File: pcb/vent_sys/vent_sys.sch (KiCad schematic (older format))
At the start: 22 parts

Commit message: deleted ds2482-100
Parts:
- removed J?: Conn_01x03_Female, symbol Connector:Conn_01x03_Female
- removed R?: R_Variable, symbol Device:R_Variable
- removed R? (x2): R, symbol Device:R
- removed U?: DS2482-100, Housings_SOIC:SOIC-8_3.9x4.9mm_Pitch1.27mm, symbol maxim:DS2482-100
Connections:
- wire segments 145 -> 115
- no-connect marks 1 -> 0
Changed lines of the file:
@@
 Wire Bus Line
 	8000 2100 10800 2100
-$Comp
-L maxim:DS2482-100 U?
-U 1 1 5C5AE47D
-P 2600 1300
-F 0 "U?" H 2600 1978 50  0000 C CNN
-F 1 "DS2482-100" H 2600 1887 50  0000 C CNN
-F 2 "Housings_SOIC:SOIC-8_3.9x4.9mm_Pitch1.27mm" H 2650 900 50  0001 L CNN
-F 3 "https://datasheets.maximintegrated.com/en/ds/DS2482-100.pdf" H 2870 1550 50  0001 C CNN
-	1    2600 1300
-	1    0    0    -1
-$EndComp
-$Comp
-L Device:R_Variable R?
-U 1 1 5C5AE99F
-P 3400 1150
-F 0 "R?" H 3528 1196 50  0000 L CNN
-F 1 "R_Variable" H 3528 1105 50  0000 L CNN
-F 2 "" V 3330 1150 50  0001 C CNN
-F 3 "~" H 3400 1150 50  0001 C CNN
-	1    3400 1150
-	1    0    0    -1
-$EndComp
-$Comp
-L Device:R R?
-U 1 1 5C5AEA85
-P 800 1000
-F 0 "R?" H 870 1046 50  0000 L CNN
-F 1 "R" H 870 955 50  0000 L CNN
-F 2 "" V 730 1000 50  0001 C CNN
-F 3 "~" H 800 1000 50  0001 C CNN
-	1    800  1000
-	1    0    0    -1
-$EndComp
-$Comp
-L Connector:Conn_01x03_Female J?
-U 1 1 5C5B0332
-P 4000 1400
-F 0 "J?" H 4027 1426 50  0000 L CNN
-F 1 "Conn_01x03_Female" H 4027 1335 50  0000 L CNN
-F 2 "" H 4000 1400 50  0001 C CNN
-F 3 "~" H 4000 1400 50  0001 C CNN
-	1    4000 1400
-	1    0    0    -1
-$EndComp
-$Comp
-L power:+3.3V #PWR?
-U 1 1 5C5B7267
-P 2950 700
-F 0 "#PWR?" H 2950 550 50  0001 C CNN
-F 1 "+3.3V" H 2965 873 50  0000 C CNN
-F 2 "" H 2950 700 50  0001 C CNN
-F 3 "" H 2950 700 50  0001 C CNN
-	1    2950 700
-	1    0    0    -1
-$EndComp
-Wire Wire Line
-	2600 800  2950 800
-Wire Wire Line
-	2950 800  2950 750
-$Comp
-L power:GND #PWR?
-U 1 1 5C5B77FB
-P 2600 1950
-F 0 "#PWR?" H 2600 1700 50  0001 C CNN
-F 1 "GND" H 2605 1777 50  0000 C CNN
-F 2 "" H 2600 1950 50  0001 C CNN
-F 3 "" H 2600 1950 50  0001 C CNN
-	1    2600 1950
-	1    0    0    -1
-$EndComp
-Wire Wire Line
-	2600 1800 2600 1850
-NoConn ~ 3100 1100
-$Comp
-L Device:R R?
-U 1 1 5C5B9E9D
-P 1400 1000
-F 0 "R?" H 1470 1046 50  0000 L CNN
-F 1 "R" H 1470 955 50  0000 L CNN
-F 2 "" V 1330 1000 50  0001 C CNN
-F 3 "~" H 1400 1000 50  0001 C CNN
-	1    1400 1000
-	1    0    0    -1
-$EndComp
-Wire Wire Line
-	1400 750  2950 750
-Connection ~ 2950 750
-Wire Wire Line
-	3400 750  2950 750
-Wire Wire Line
-	2950 750  2950 700
-Wire Wire Line
-	1400 850  1400 750
-Connection ~ 1400 750
-Wire Wire Line
-	800  750  1400 750
-Wire Wire Line
-	2100 1100 1700 1100
-Wire Wire Line
-	1700 1100 1700 1150
-Wire Wire Line
-	1700 1150 1400 1150
-Wire Wire Line
-	800  850  800  750
-Wire Wire Line
-	800  1150 800  1250
-Wire Wire Line
-	800  1250 1900 1250
-Wire Wire Line
-	1900 1250 1900 1200
-Wire Wire Line
-	1900 1200 2100 1200
-$Comp
-L power:GND #PWR?
-U 1 1 5C5C0A5C
-P 1600 1550
-F 0 "#PWR?" H 1600 1300 50  0001 C CNN
-F 1 "GND" H 1605 1377 50  0000 C CNN
-F 2 "" H 1600 1550 50  0001 C CNN
-F 3 "" H 1600 1550 50  0001 C CNN
-	1    1600 1550
-	1    0    0    -1
-$EndComp
-Wire Wire Line
-	2100 1400 1600 1400
-Wire Wire Line
-	1600 1400 1600 1500
-Wire Wire Line
-	2100 1500 1600 1500
-Connection ~ 1600 1500
-Wire Wire Line
-	1600 1500 1600 1550
-Wire Wire Line
-	3400 1000 3400 750
-Connection ~ 3400 750
-Wire Wire Line
-	3700 750  3400 750
-Wire Wire Line
-	3100 1400 3400 1400
-Wire Wire Line
-	3400 1400 3400 1300
-Connection ~ 3400 1400
-Wire Wire Line
-	3800 1400 3400 1400
-Wire Wire Line
-	3800 1500 3800 1850
-Wire Wire Line
-	3800 1850 2600 1850
-Connection ~ 2600 1850
-Wire Wire Line
-	2600 1850 2600 1950
-Wire Wire Line
-	3800 1300 3700 1300
-Wire Wire Line
-	3700 1300 3700 750
 $EndSCHEMATC

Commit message: connect RA02
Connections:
- net Reset: now reaches U?.26 (A1)
- net Reset: now also U?.4 (reset)
- net nIRQ: now reaches U?.27 (A2/U2TX)
- net nIRQ: now also U?.5 (dio0)
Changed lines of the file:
@@
 Text Label 4200 1700 0    50   ~ 0
 Herz_counter
+Entry Wire Line
+	9200 2100 9300 2200
+Wire Wire Line
+	8500 1200 8000 1200
+Wire Wire Line
+	8000 1200 8000 2000
+Entry Wire Line
+	8000 2000 8100 2100
+Text Label 7300 3800 0    50   ~ 0
+Reset
+Text Label 8050 1200 0    50   ~ 0
+Reset
+Wire Wire Line
+	6750 3800 9300 3800
+Wire Wire Line
+	9300 3800 9300 2200
+Entry Wire Line
+	9100 2100 9200 2200
+Wire Wire Line
+	9200 2200 9200 3650
+Wire Wire Line
+	9200 3650 6750 3650
+Text Label 7300 3650 0    50   ~ 0
+nIRQ
+Wire Wire Line
+	8500 1300 8150 1300
+Wire Wire Line
+	8150 1300 8150 2000
 Wire Bus Line
 	10800 750  10800 2100
 Wire Bus Line
 	8000 2100 10800 2100
+Entry Wire Line
+	8150 2000 8250 2100
+Text Label 8200 1300 0    50   ~ 0
+nIRQ
 $EndSCHEMATC

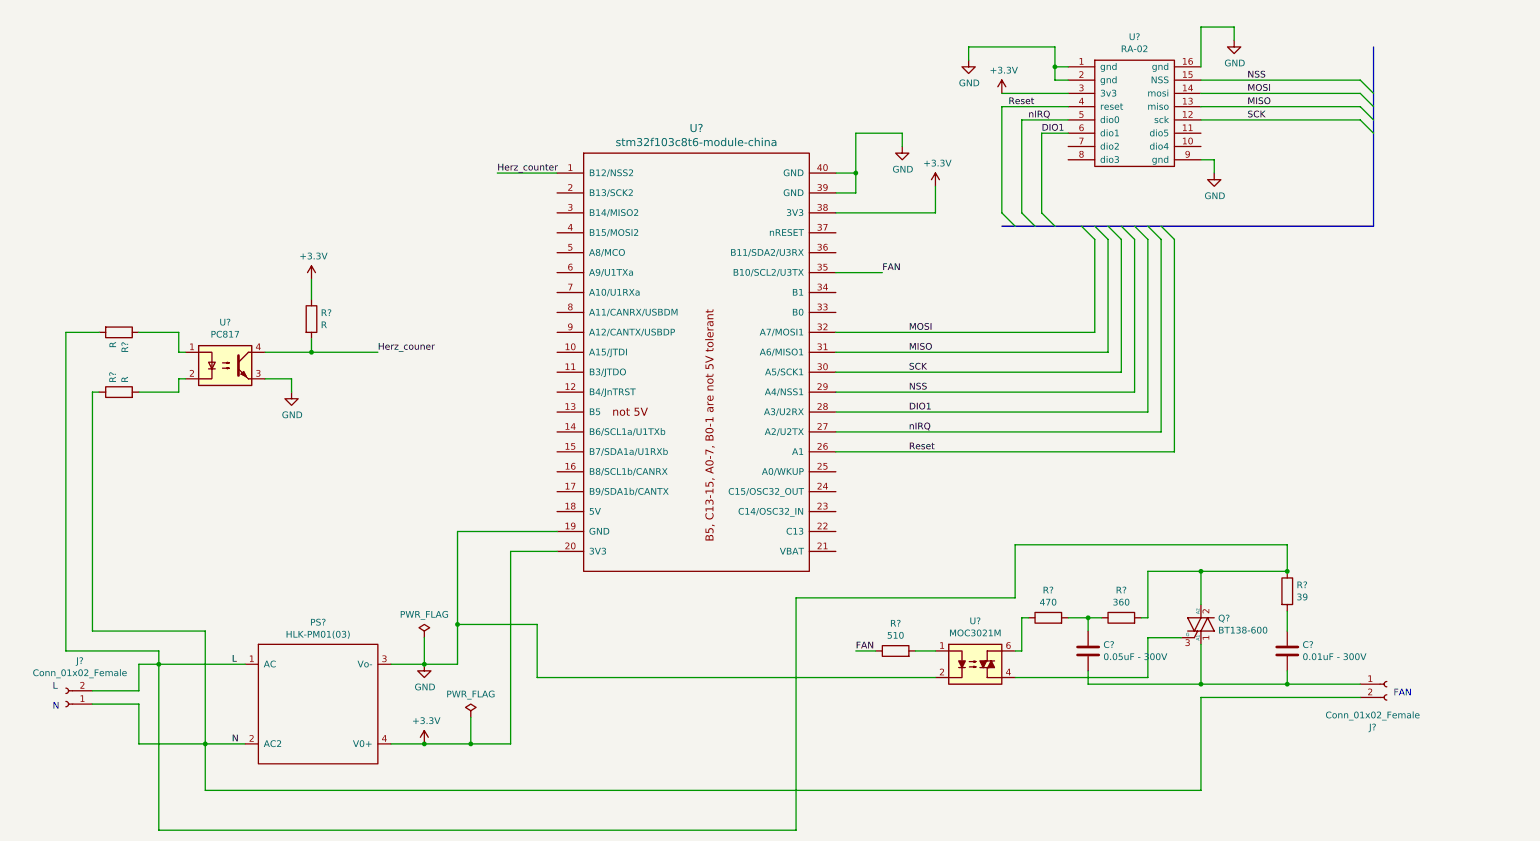
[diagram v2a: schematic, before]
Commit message: add unique identifiers
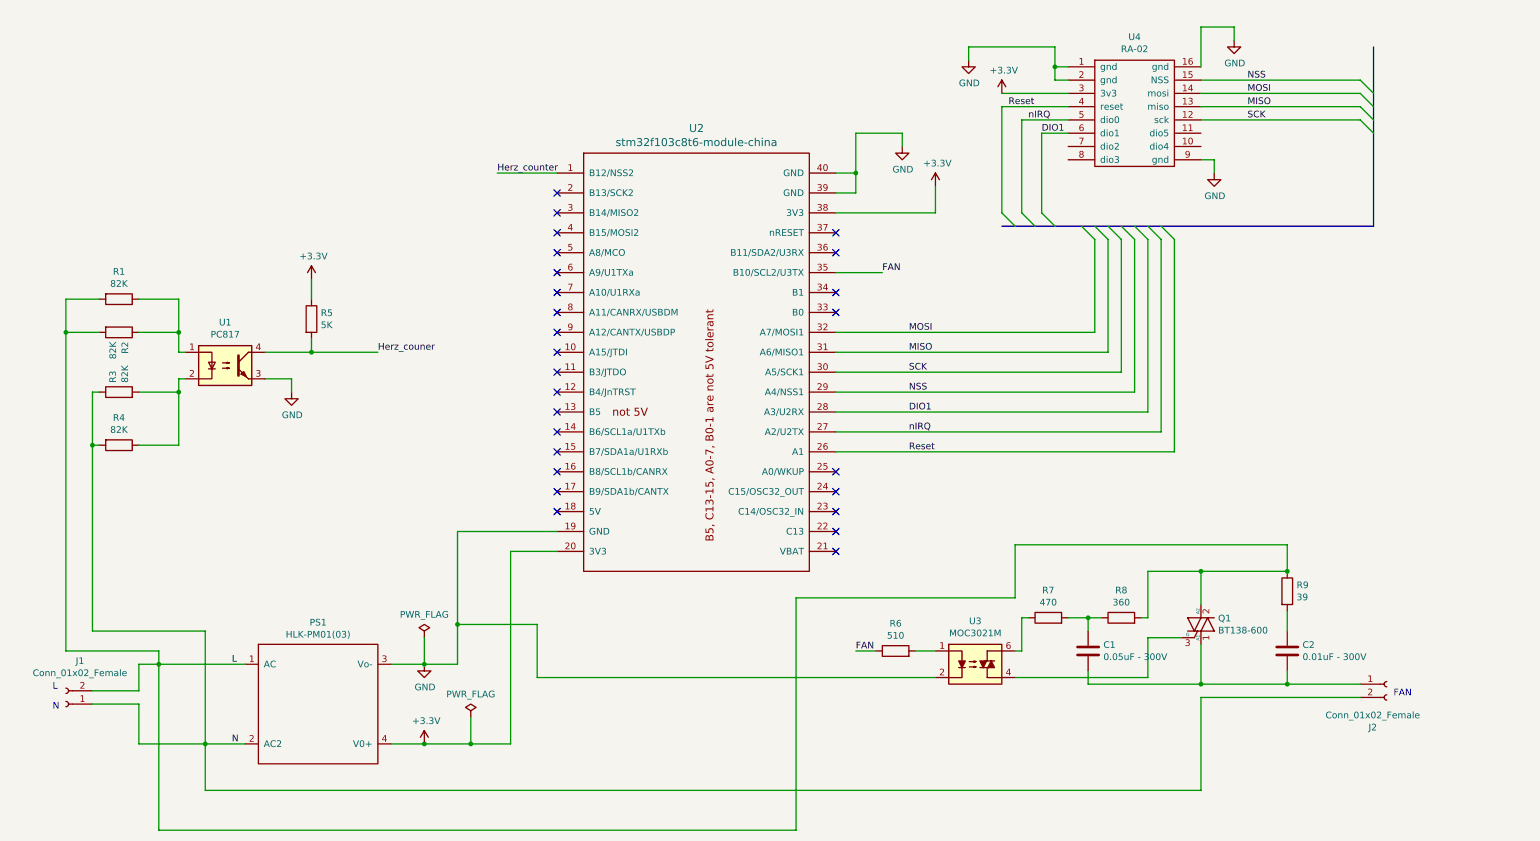
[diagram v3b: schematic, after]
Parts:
- added R1, R4: 82K, Resistor_THT:R_Axial_DIN0207_L6.3mm_D2.5mm_P10.16mm_Horizontal, symbol Device:R
- PS1: renamed from PS?; footprint (none) -> HLK-PM01:HLK-PM01
- R2, R3: renamed from R?; value R -> 82K; footprint (none) -> Resistor_THT:R_Axial_DIN0207_L6.3mm_D2.5mm_P10.16mm_Horizontal
- R5: renamed from R?; value R -> 5K; footprint (none) -> Resistor_SMD:R_0805_2012Metric_Pad1.15x1.40mm_HandSolder
- U2: renamed from U?; footprint myelin-kicad:stm32f103c8t6-module-china -> (none)
- U4: renamed from U?; footprint (none) -> RF_Module:Ai-Thinker-Ra-01-LoRa
- gave numbers to parts that had none: 11
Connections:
- net L: now also R1.2
- net N: now also R4.2
- net at R2.1, U1.1: now also R1.1
- net at R3.2, U1.2: now also R4.1
- no-connect marks 0 -> 26

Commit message: electrical rules check are OK
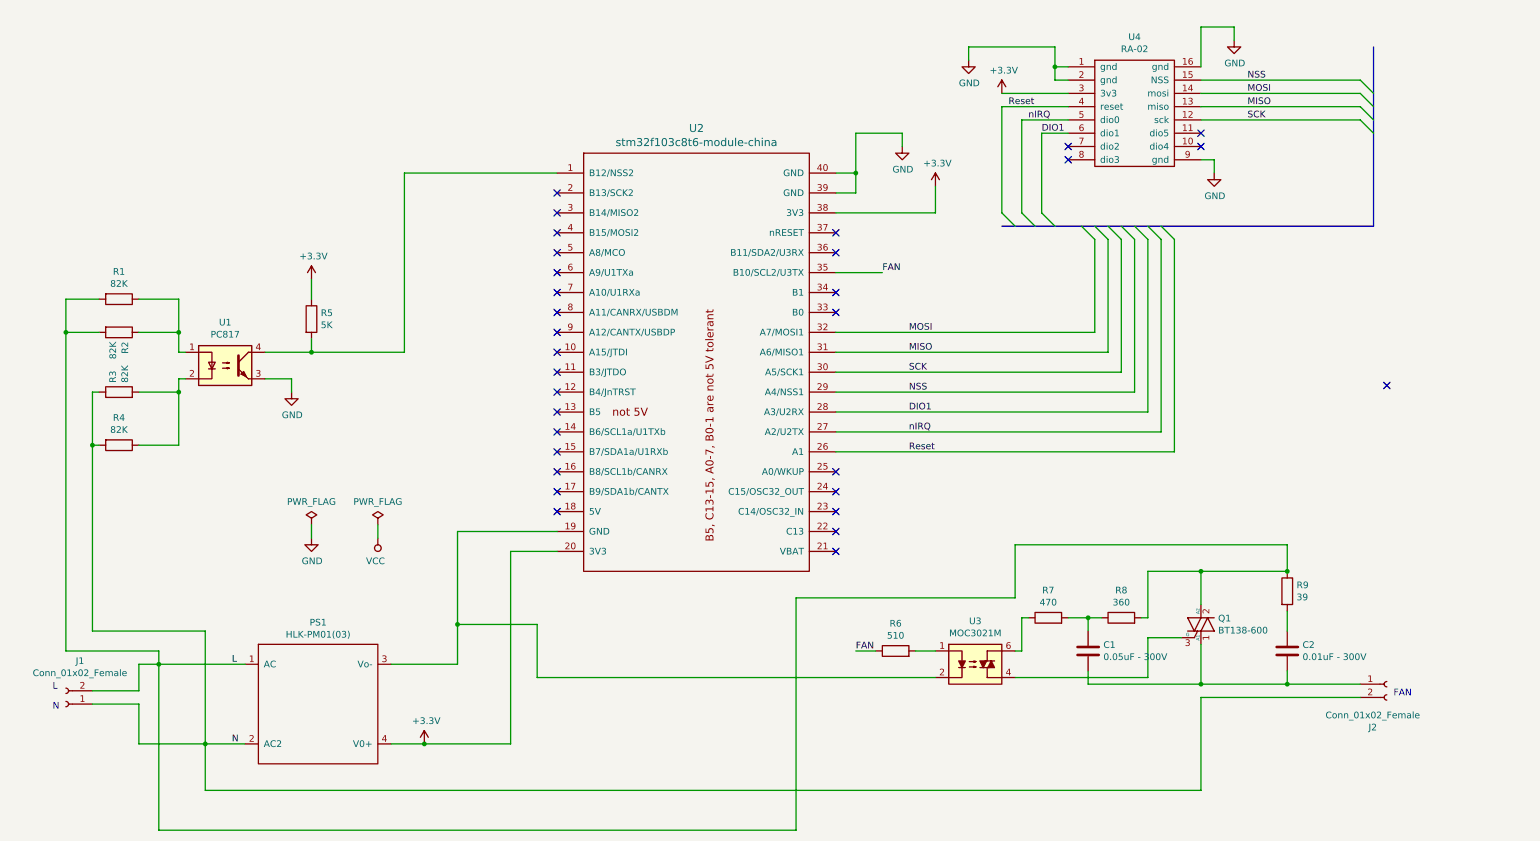
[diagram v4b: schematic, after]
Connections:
- net Herz_counter is gone; now on an unnamed net: U2.1 (B12/NSS2)
- net GND: no longer PS1.3 (Vo-), U2.19 (GND), U3.2
- net Herz_couner: no longer names the net of R5.2, U1.4
- new net: PS1.3 (Vo-), U2.19 (GND), U3.2
- no-connect marks 26 -> 31
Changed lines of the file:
@@
-$EndComp
-$Comp
-L power:GND #PWR03
-U 1 1 5C5AFA20
-P 3650 5400
-F 0 "#PWR03" H 3650 5150 50  0001 C CNN
-F 1 "GND" H 3655 5227 50  0000 C CNN
-F 2 "" H 3650 5400 50  0001 C CNN
-F 3 "" H 3650 5400 50  0001 C CNN
-	1    3650 5400
-	1    0    0    -1
 $EndComp
 $Comp
@@
 Wire Wire Line
 	3400 6000 3650 6000
-Wire Wire Line
-	3400 5400 3650 5400
 $Comp
 L Connector:Conn_01x02_Female J1
@@
 Wire Wire Line
 	4300 4550 4300 6000
-Wire Wire Line
-	4300 6000 4000 6000
 Connection ~ 3650 6000
 $Comp
@@
 	3900 4400 3900 5100
 Wire Wire Line
-	3900 5400 3650 5400
-Connection ~ 3650 5400
-Wire Wire Line
 	1800 2900 1800 3050
 Wire Wire Line
@@
 L power:PWR_FLAG #FLG02
 U 1 1 5C8AB50F
-P 4000 5800
-F 0 "#FLG02" H 4000 5875 50  0001 C CNN
-F 1 "PWR_FLAG" H 4000 5974 50  0000 C CNN
-F 2 "" H 4000 5800 50  0001 C CNN
-F 3 "~" H 4000 5800 50  0001 C CNN
-	1    4000 5800
+P 2800 4350
+F 0 "#FLG02" H 2800 4425 50  0001 C CNN
+F 1 "PWR_FLAG" H 2800 4524 50  0000 C CNN
+F 2 "" H 2800 4350 50  0001 C CNN
+F 3 "~" H 2800 4350 50  0001 C CNN
+	1    2800 4350
 	1    0    0    -1
 $EndComp
@@
 L power:PWR_FLAG #FLG01
 U 1 1 5C8AB681
-P 3650 5200
-F 0 "#FLG01" H 3650 5275 50  0001 C CNN
-F 1 "PWR_FLAG" H 3650 5374 50  0000 C CNN
-F 2 "" H 3650 5200 50  0001 C CNN
-F 3 "~" H 3650 5200 50  0001 C CNN
-	1    3650 5200
-	1    0    0    -1
-$EndComp
-Wire Wire Line
-	4000 5800 4000 6000
-Connection ~ 4000 6000
-Wire Wire Line
-	4000 6000 3650 6000
-Wire Wire Line
-	3650 5200 3650 5400
+P 3300 4350
+F 0 "#FLG01" H 3300 4425 50  0001 C CNN
+F 1 "PWR_FLAG" H 3300 4524 50  0000 C CNN
+F 2 "" H 3300 4350 50  0001 C CNN
+F 3 "~" H 3300 4350 50  0001 C CNN
+	1    3300 4350
+	1    0    0    -1
+$EndComp
 Text Label 7300 2900 0    50   ~ 0
 MOSI
@@
 Wire Wire Line
 	3900 5100 3900 5400
-Wire Wire Line
-	3300 3050 2800 3050
 Connection ~ 2800 3050
-Text Label 3300 3050 0    50   ~ 0
-Herz_couner
-Wire Wire Line
-	4650 1700 4200 1700
-Text Label 4200 1700 0    50   ~ 0
-Herz_counter
 Entry Wire Line
 	9200 2100 9300 2200
@@
 NoConn ~ 6750 2300
 NoConn ~ 6750 2150
+NoConn ~ 10900 3300
+Wire Wire Line
+	3650 6000 4300 6000
+$Comp
+L power:GND #PWR0101
+U 1 1 5C9B68E2
+P 2800 4450
+F 0 "#PWR0101" H 2800 4200 50  0001 C CNN
+F 1 "GND" H 2805 4277 50  0000 C CNN
+F 2 "" H 2800 4450 50  0001 C CNN
+F 3 "" H 2800 4450 50  0001 C CNN
+	1    2800 4450
+	1    0    0    -1
+$EndComp
+Wire Wire Line
+	2800 4350 2800 4450
+$Comp
+L power:VCC #PWR0102
+U 1 1 5C9BB0DE
+P 3300 4450
+F 0 "#PWR0102" H 3300 4300 50  0001 C CNN
+F 1 "VCC" H 3318 4623 50  0000 C CNN
+F 2 "" H 3300 4450 50  0001 C CNN
+F 3 "" H 3300 4450 50  0001 C CNN
+	1    3300 4450
+	-1   0    0    1
+$EndComp
+Wire Wire Line
+	3300 4350 3300 4450
+NoConn ~ 9500 1400
+NoConn ~ 9500 1500
+NoConn ~ 8500 1500
+NoConn ~ 8500 1600
+Wire Wire Line
+	3400 5400 3900 5400
+Wire Wire Line
+	4650 1700 3500 1700
+Wire Wire Line
+	3500 1700 3500 3050
+Wire Wire Line
+	2800 3050 3500 3050
 Wire Bus Line
 	10800 750  10800 2100
